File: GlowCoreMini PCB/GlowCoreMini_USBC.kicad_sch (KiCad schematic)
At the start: 5 parts

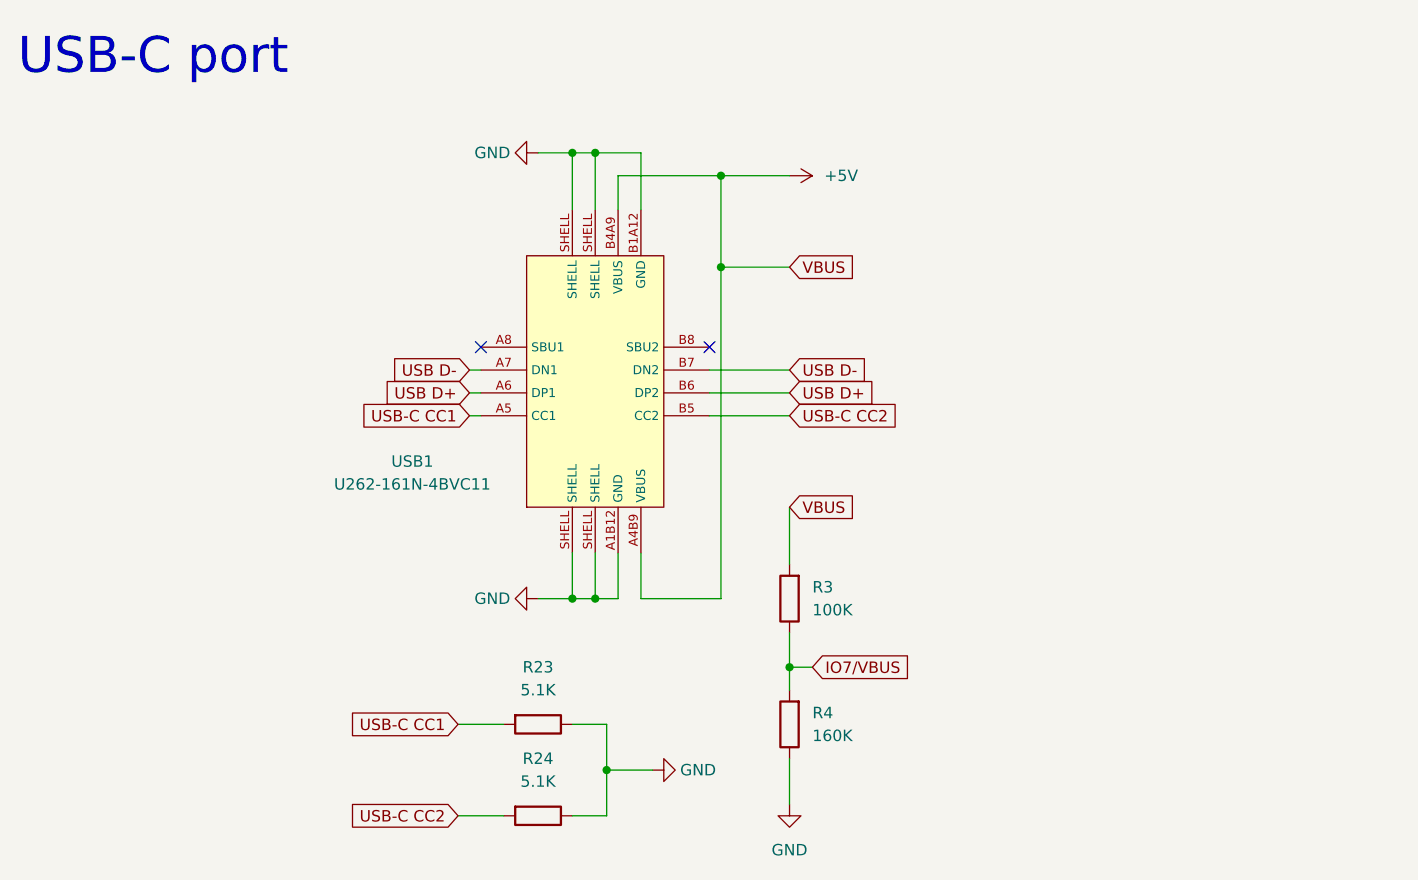
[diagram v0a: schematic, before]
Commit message: split up schematic
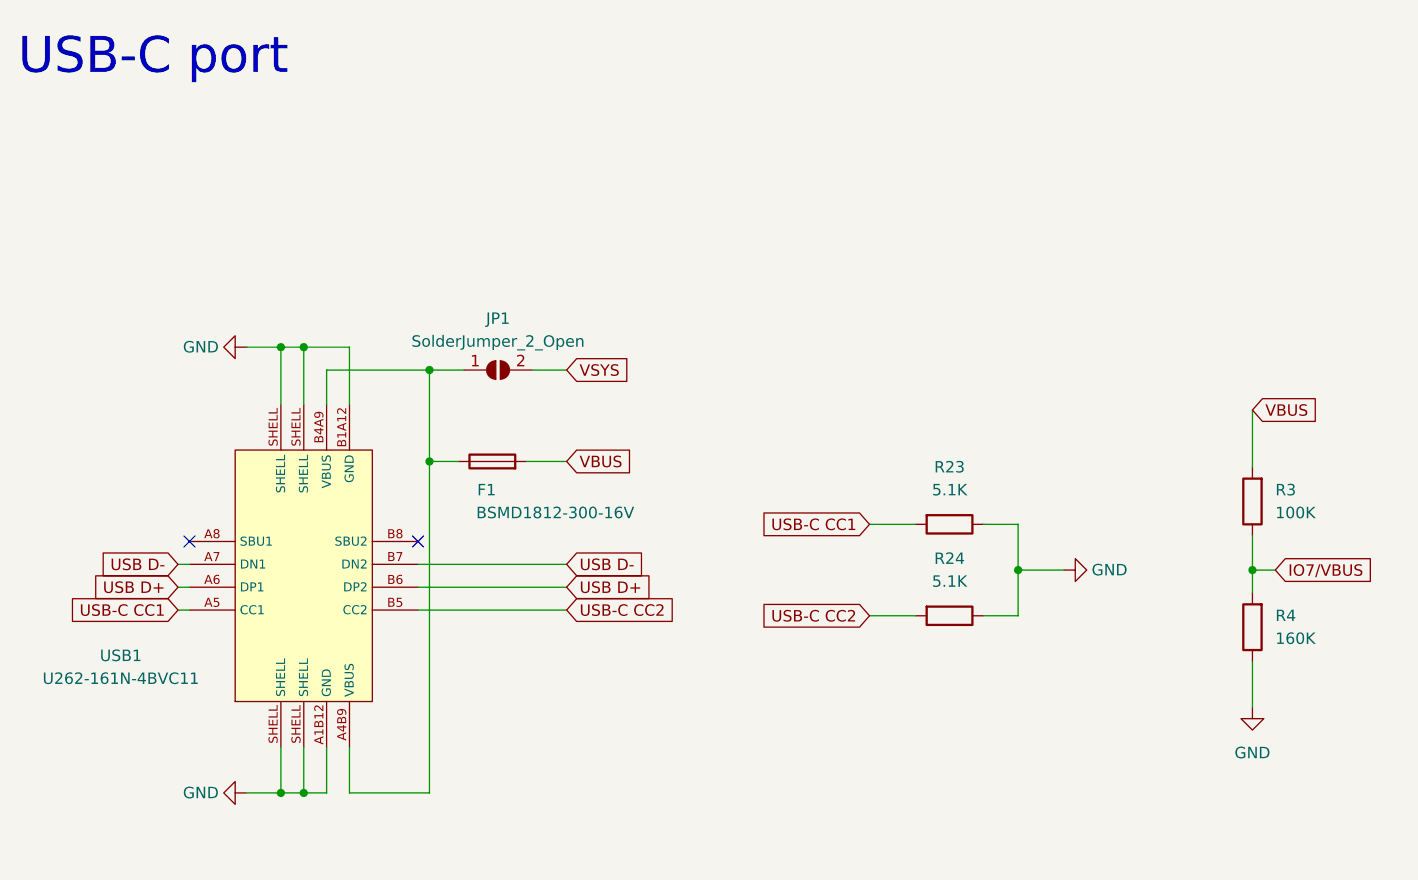
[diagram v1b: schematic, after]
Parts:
- added F1: BSMD1812-300-16V, Fuse:Fuse_1812_4532Metric_Pad1.30x3.40mm_HandSolder, symbol Device:Fuse
- added JP1: SolderJumper_2_Open, Jumper:SolderJumper-2_P1.3mm_Open_RoundedPad1.0x1.5mm, symbol Jumper:SolderJumper_2_Open
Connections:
- net +5V: no longer names the net of USB1.A4B9 (VBUS), USB1.B4A9 (VBUS)
- net +5V: now also F1.1, JP1.1 (A); no longer R3.2
- new net VBUS: F1.2, R3.2
- new net VSYS: JP1.2 (B)
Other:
- moved on the sheet: R23, R24, R3, R4, USB1
